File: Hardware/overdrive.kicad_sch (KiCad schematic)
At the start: 15 parts, among them U1 TL072

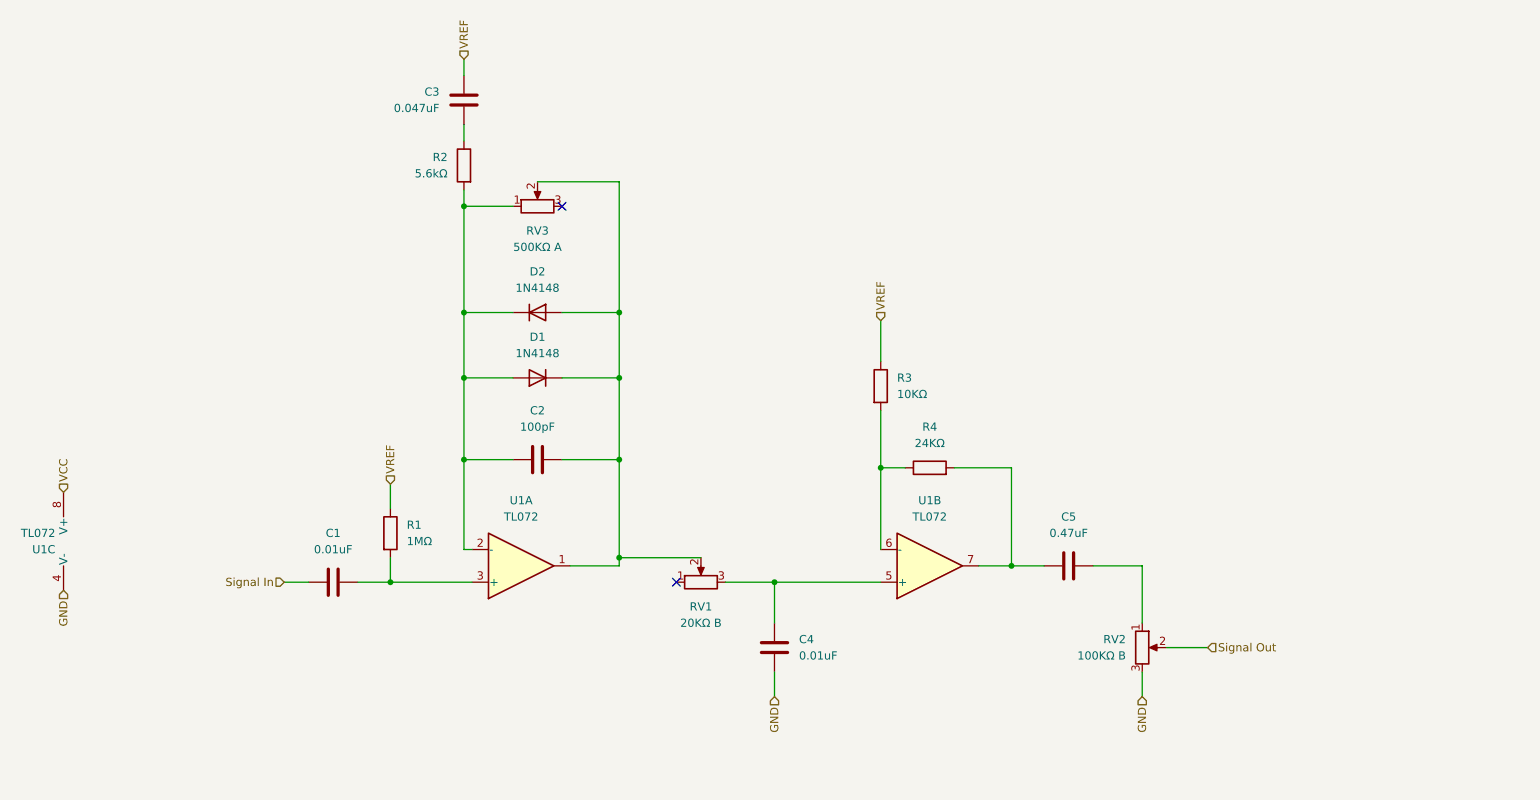
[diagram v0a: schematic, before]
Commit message: Add Octaver and Reverb effects
Added the schematics for the octaver and reverb effects, also fixed up some minor things on the overdrive schematic.
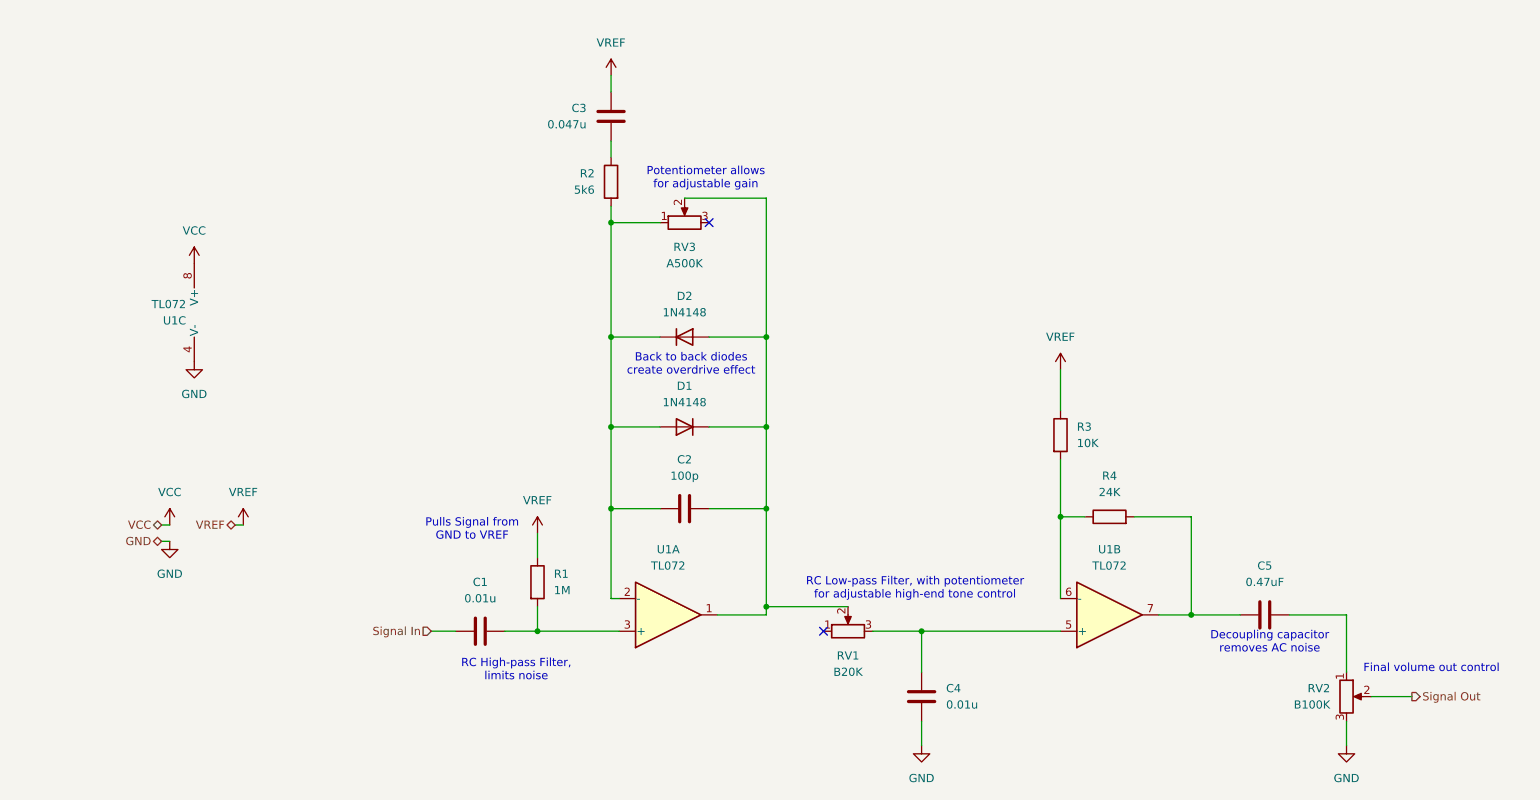
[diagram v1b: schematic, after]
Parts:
- C1, C4: value 0.01uF -> 0.01u
- C2: value 100pF -> 100p
- C3: value 0.047uF -> 0.047u
- R1: value 1MΩ -> 1M
- R2: value 5.6kΩ -> 5k6
- R3: value 10KΩ -> 10K
- R4: value 24KΩ -> 24K
- RV1: value 20KΩ B -> B20K
- RV2: value 100KΩ B -> B100K
- RV3: value 500KΩ A -> A500K
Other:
- note added: "Back to back diodes create overdrive effect"
- note added: "Decoupling capacitor removes AC noise"
- note added: "Final volume out control"
- note added: "Potentiometer allows for adjustable gain"
- note added: "Pulls Signal from GND to VREF"
- note added: "RC High-pass Filter, limits noise"
- note added: "RC Low-pass Filter, with potentiometer for adjustable high-end tone control"
- moved on the sheet: C1, C2, C3, C4, C5, D1, D2, R1, R2, R3, R4, RV1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
